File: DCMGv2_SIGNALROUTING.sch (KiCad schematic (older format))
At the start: 320 parts, among them P1 BRANCH 1 BUS 1 LOAD3 NC, P10 BRANCH 1 BUS 1 LOAD 2 NC, P100 CONNECTOR, P101 CONNECTOR, P102 CONNECTOR, P103 CONNECTOR, P104 CONNECTOR, P105 CONNECTOR, P106 CONNECTOR, P107 CONNECTOR, P108 CONNECTOR, P109 CONNECTOR, P11 BRANCH 1 BUS 1 LOAD 1 NO, P110 CONNECTOR, P111 CONNECTOR, P112 CONNECTOR, P113 CONNECTOR, P114 CONNECTOR, P115 CONNECTOR, P116 CONNECTOR, P117 CONNECTOR, P118 CONNECTOR, P119 CONNECTOR, P12 BRANCH 1 BUS 1 LOAD 1 NC, P120 CONNECTOR, P121 CONNECTOR, P122 CONNECTOR, P123 CONNECTOR, P124 CONNECTOR, P125 CONNECTOR, P126 CONNECTOR, P127 CONNECTOR, P128 CONNECTOR, P129 CONNECTOR, P13 BRANCH 2 BUS 1 LOAD 1 NO, P130 CONNECTOR, P131 CONNECTOR, P132 CONNECTOR, P133 CONNECTOR, P134 CONNECTOR, P135 CONNECTOR, P136 CONNECTOR, P137 CONNECTOR, P138 CONNECTOR, P139 CONNECTOR, P14 BRANCH 2 BUS 1 DISTAL NC, P140 CONNECTOR, P141 CONNECTOR, P142 CONNECTOR, P143 CONNECTOR, P144 CONNECTOR, P145 CONNECTOR, P146 CONNECTOR, P147 CONNECTOR, P148 CONNECTOR, P149 CONNECTOR, P15 BRANCH 2 BUS 1 DISTAL USER, P150 CONNECTOR, P151 CONNECTOR, P152 CONNECTOR, P153 CONNECTOR, P154 CONNECTOR, P155 CONNECTOR, P156 CONNECTOR, P157 CONNECTOR, P158 CONNECTOR, P159 CONNECTOR, P16 BRANCH 2 BUS 1 DISTAL NO, P160 CONNECTOR, P161 CONNECTOR, P162 CONNECTOR, P163 CONNECTOR, P164 CONNECTOR, P165 CONNECTOR, P166 CONNECTOR, P167 CONNECTOR, P168 CONNECTOR, P169 CONNECTOR, P17 BRANCH 2 BUS 1 PROXIMAL NC, P170 CONNECTOR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

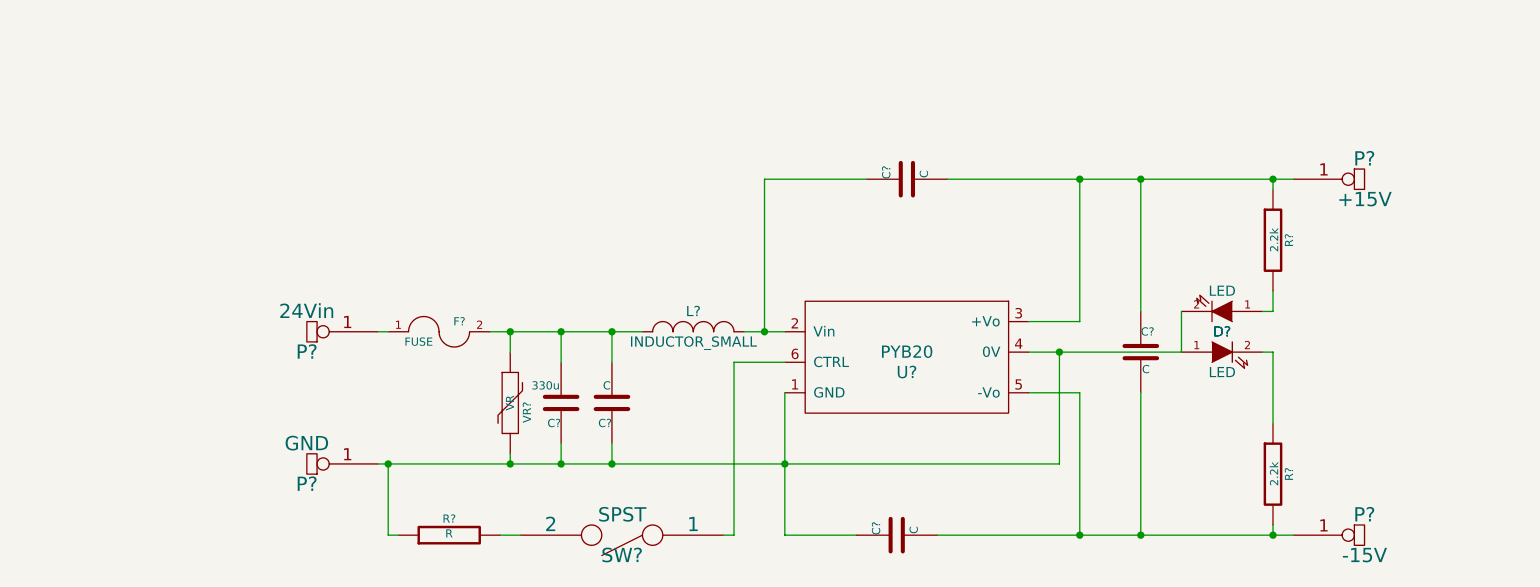
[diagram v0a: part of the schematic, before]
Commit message: replaced SPST slider footprint. More importantly, I fixed the following issues from the prototype test source board: 1. over current protection transistor drain and source were reversed. 2. U12 negative supply disconnected. 3. screw terminals inaccessible with daughterboard in place. 4. lack of reverse bias protection.
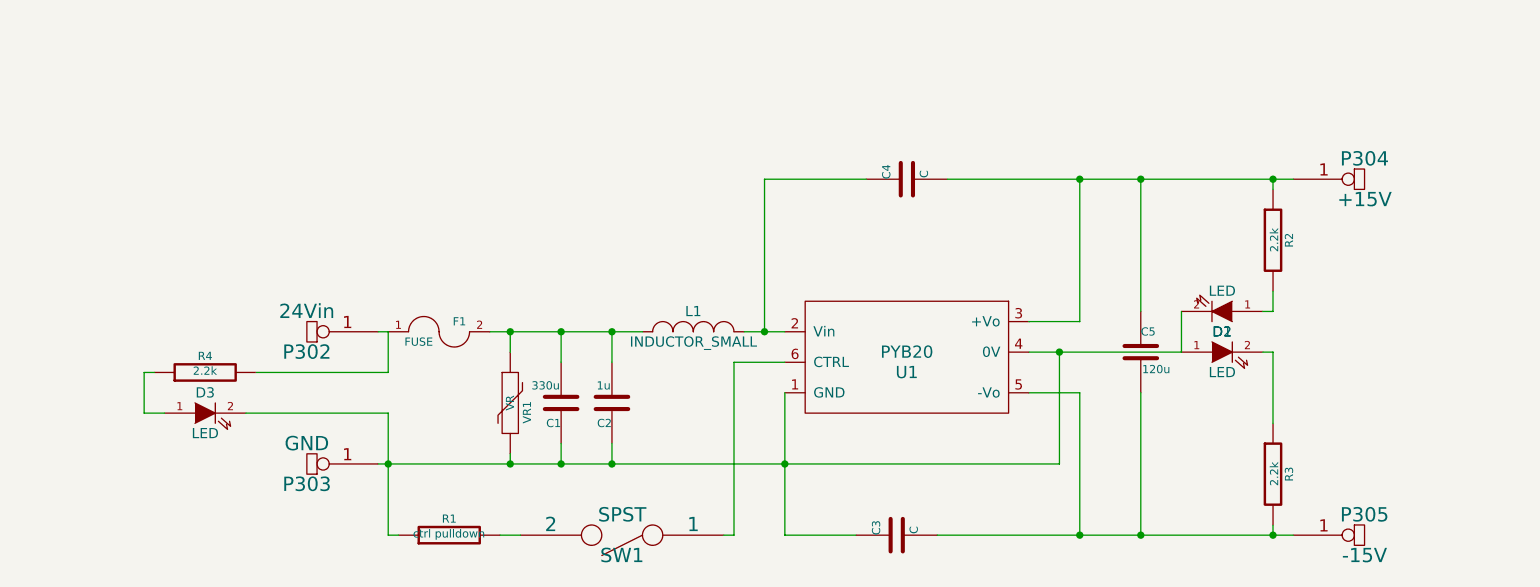
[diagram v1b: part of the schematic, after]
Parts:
- added D3: LED, ~, symbol LED
- added R4: 2.2k, ~, symbol R
- C2: renamed from C?; value C -> 1u
- C5: renamed from C?; value C -> 120u
- R1: renamed from R?; value R -> ctrl pulldown
- gave numbers to parts that had none: 16
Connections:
- net at C1.1, C2.1, C3.1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: now also D3.2 (K)
- net at F1.1, P302.1 (W): now also R4.2
- new net: D3.1 (A), R4.1
